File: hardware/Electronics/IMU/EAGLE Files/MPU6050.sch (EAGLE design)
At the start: 8 parts, among them U1 MPU-6050

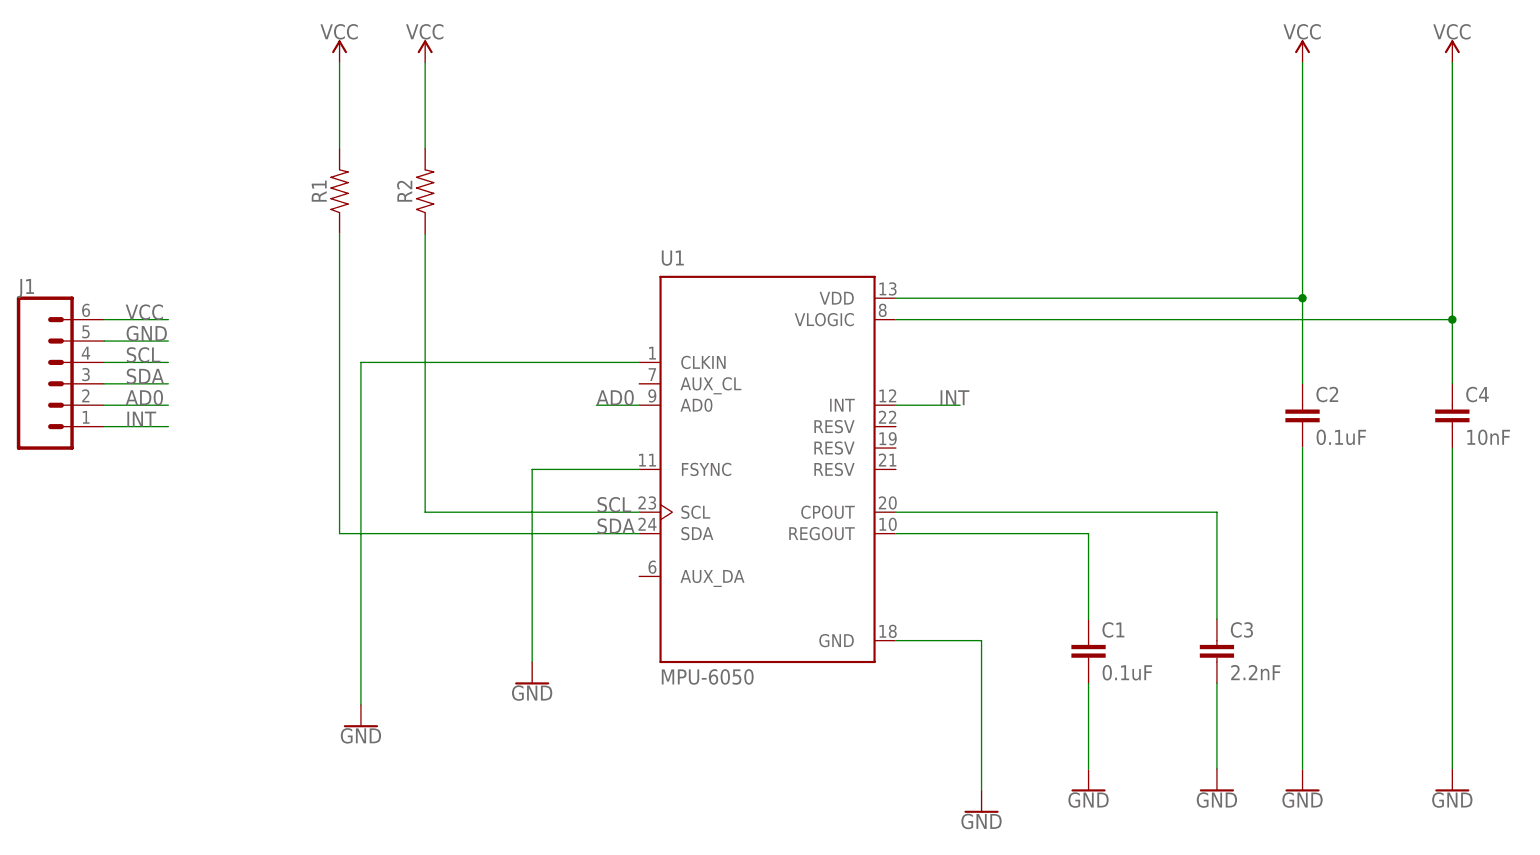
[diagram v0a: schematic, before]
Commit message: Added IMU and Integration board schematic and layout PNG's
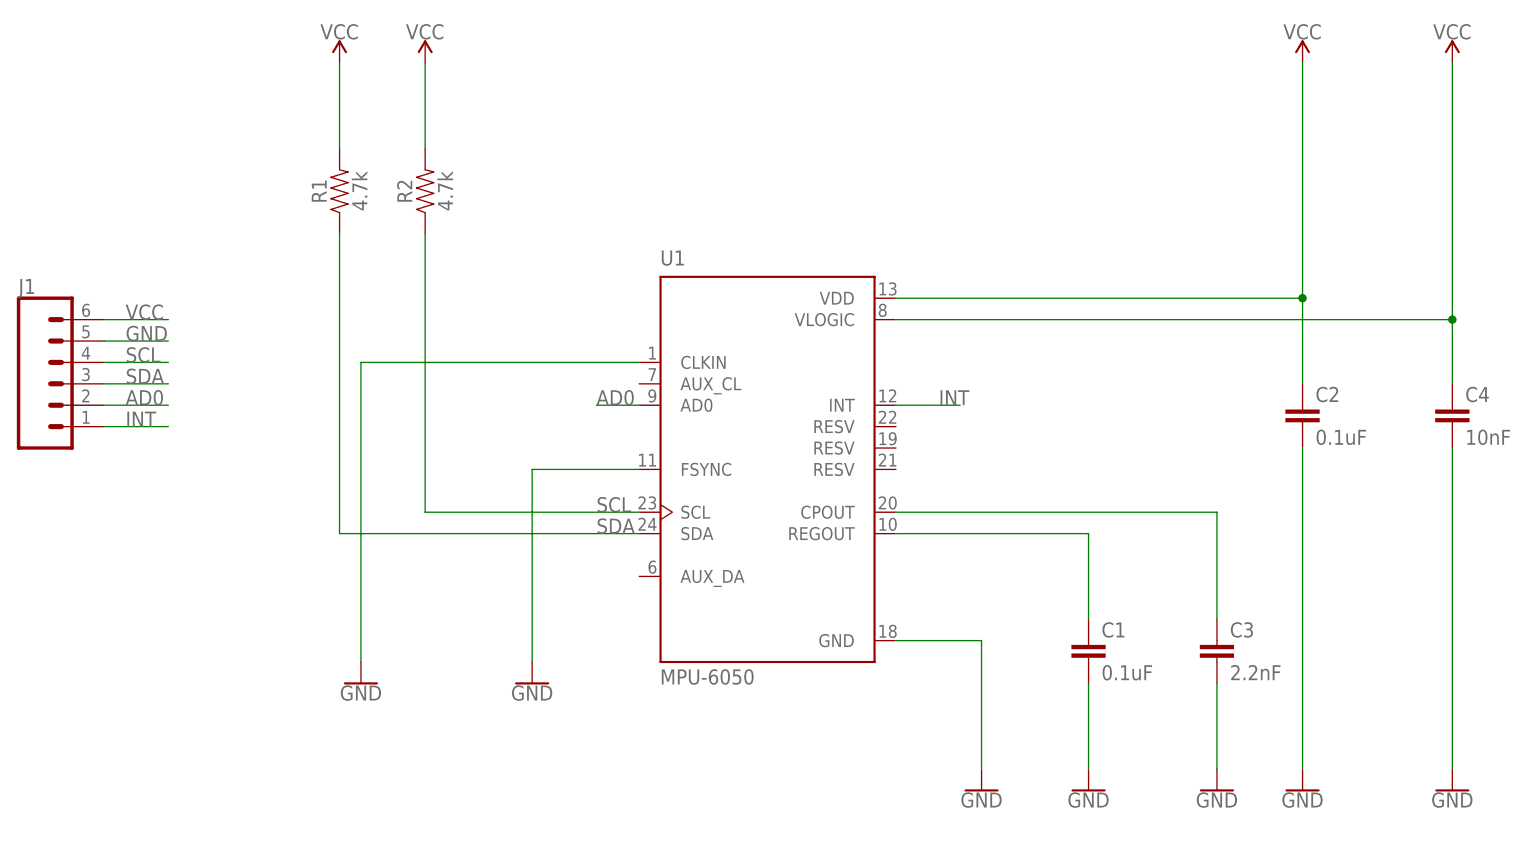
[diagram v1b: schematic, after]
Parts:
- R1, R2: value (none) -> 4.7k
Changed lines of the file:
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@@
 <part name="GND6" library="SparkFun-PowerSymbols" deviceset="GND" device=""/>
 <part name="GND7" library="SparkFun-PowerSymbols" deviceset="GND" device=""/>
-<part name="R1" library="SparkFun-Resistors" deviceset="RESISTOR" device="0805" value=" "/>
-<part name="R2" library="SparkFun-Resistors" deviceset="RESISTOR" device="0805" value=" "/>
+<part name="R1" library="SparkFun-Resistors" deviceset="RESISTOR" device="0805" value="4.7k"/>
+<part name="R2" library="SparkFun-Resistors" deviceset="RESISTOR" device="0805" value="4.7k"/>
 <part name="C1" library="SparkFun-Capacitors" deviceset="1.0UF" device="-0805-25V-10%" value="0.1uF"/>
 <part name="C3" library="SparkFun-Capacitors" deviceset="1.0UF" device="-0805-25V-10%" value="2.2nF"/>
@@
 <attribute name="VALUE" x="50.8" y="17.526" size="1.778" layer="96" align="top-center"/>
 </instance>
-<instance part="GND6" gate="1" x="104.14" y="2.54" smashed="yes">
-<attribute name="VALUE" x="104.14" y="2.286" size="1.778" layer="96" align="top-center"/>
+<instance part="GND6" gate="1" x="104.14" y="5.08" smashed="yes">
+<attribute name="VALUE" x="104.14" y="4.826" size="1.778" layer="96" align="top-center"/>
 </instance>
-<instance part="GND7" gate="1" x="30.48" y="12.7" smashed="yes">
-<attribute name="VALUE" x="30.48" y="12.446" size="1.778" layer="96" align="top-center"/>
+<instance part="GND7" gate="1" x="30.48" y="17.78" smashed="yes">
+<attribute name="VALUE" x="30.48" y="17.526" size="1.778" layer="96" align="top-center"/>
 </instance>
 <instance part="R1" gate="G$1" x="27.94" y="76.2" smashed="yes" rot="R90">
@@
 <pinref part="U1" gate="G$1" pin="GND"/>
 <wire x1="93.98" y1="22.86" x2="104.14" y2="22.86" width="0.1524" layer="91"/>
-<wire x1="104.14" y1="22.86" x2="104.14" y2="5.08" width="0.1524" layer="91"/>
+<wire x1="104.14" y1="22.86" x2="104.14" y2="7.62" width="0.1524" layer="91"/>
 <pinref part="GND6" gate="1" pin="GND"/>
 </segment>
@@
 <pinref part="U1" gate="G$1" pin="CLKIN"/>
 <wire x1="63.5" y1="55.88" x2="30.48" y2="55.88" width="0.1524" layer="91"/>
-<wire x1="30.48" y1="55.88" x2="30.48" y2="15.24" width="0.1524" layer="91"/>
+<wire x1="30.48" y1="55.88" x2="30.48" y2="20.32" width="0.1524" layer="91"/>
 <pinref part="GND7" gate="1" pin="GND"/>
 </segment>
